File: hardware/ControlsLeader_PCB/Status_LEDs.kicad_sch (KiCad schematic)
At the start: 0 parts

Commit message: Schematic Backup
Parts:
- added D1, D10, D11, D12, D13, D14, D15, D2, D3, D4, D5, D6, D7, D8, D9: 0805_SMD, symbol Device:LED
- added D16: Controls_PWR, symbol Device:LED
- added D18: BPS_Fault, symbol Device:LED
- added D19: Controls_HB, symbol Device:LED
- added R30, R33, R34, R35, R36, R37, R38, R39, R40, R41, R42, R43, R44, R45, R46, R47, R49, R50: 10.6k, symbol Device:R
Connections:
- new net: D12.1 (K), R43.1
- new net: D5.1 (K), R36.1
- new net: D6.1 (K), R37.1
- new net: D2.1 (K), R33.1
- new net: D19.1 (K), R50.1
- new net: D4.1 (K), R35.1
- new net: D9.1 (K), R40.1
- new net: D15.1 (K), R46.1
- new net: D10.1 (K), R41.1
- new net: D7.1 (K), R38.1
- new net: D18.1 (K), R49.1
- new net: D11.1 (K), R42.1
- new net: D8.1 (K), R39.1
- new net: D14.1 (K), R45.1
- new net: D16.1 (K), R47.1
- new net: D13.1 (K), R44.1
- new net: D3.1 (K), R34.1
- new net: D1.1 (K), R30.1
- new net BPS_Fault_PWM: D16.2 (A), D18.2 (A), D19.2 (A)
- new net Cruise_Enable_GPIO_IN: D13.2 (A)
- new net Cruise_Set_GPIO_IN: D12.2 (A)
- new net Fwd_SW_GPIO: D3.2 (A)
- new net GND: R30.2, R33.2, R34.2, R35.2, R36.2, R37.2, R38.2, R39.2, R40.2, R41.2, R42.2, R43.2, R44.2, R45.2, R46.2, R47.2, R49.2, R50.2
- new net Hazard_GPIO_IN: D15.2 (A)
- new net Horn_24V_Signal_Out: D7.2 (A)
- new net Horn_GPIO_IN: D8.2 (A)
- new net Horn_GPIO_OUT: D9.2 (A)
- new net Ign_OFF_GPIO: D6.2 (A)
- new net Ign_arr_GPIO: D1.2 (A)
- new net Ign_mtr_GPIO: D2.2 (A)
- new net Left_Blinker_ON: D10.2 (A)
- new net Neutral_Gear_GPIO: D5.2 (A)
- new net Regen_Enable_GPIO_IN: D14.2 (A)
- new net Rev_SW_GPIO: D4.2 (A)
- new net Right_Blinker_ON: D11.2 (A)

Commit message: DONE!!! - just need to add footprints + part #s)
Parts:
- removed D19: Controls_HB, symbol Device:LED
- removed R49, R50: 10.6k, symbol Device:R
- added 3.3V1: TestPoint, TestPoint:TestPoint_Pad_1.0x1.0mm, symbol Connector:TestPoint
- added C15, C16: 10uF, Capacitor_SMD:C_0805_2012Metric_Pad1.18x1.45mm_HandSolder, symbol Device:C
- added D17, D26, D27, D28, D29: 0603_SMD, symbol Device:LED
- added J5: BPS_Fault_LED, Connector_Molex:Molex_Micro-Fit_3.0_43650-0300_1x03_P3.00mm_Horizontal, symbol Connector_Generic:Conn_01x03
- added R16, R17: 20, symbol Device:R
- added R55, R56, R57, R58: 120, symbol Device:R
- added U4: LT1963AEST-3.3#TRPBF, Package_TO_SOT_SMD:SOT-223-3_TabPin2, symbol Regulator_Linear:LT1963AxST-3.3
- D1, D10, D11, D12, D13, D14, D15, D2, D3, D4, D5, D6, D7, D8, D9: value 0805_SMD -> 0603_SMD
- D16: value Controls_PWR -> 0603_SMD
- D18: value BPS_Fault -> 0603_SMD
- R30, R33, R34, R35, R36, R37, R38, R39, R40, R41, R42, R43, R44: value 10.6k -> 20
- R45, R46: value 10.6k -> 120
- R47: value 10.6k -> 1.1k
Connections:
- net GND: now also C15.2, C16.2, J5.1 (Pin_1), R16.2, R17.2, R55.2, R56.2, R57.2, R58.2, U4.2 (GND)
- net at D12.1 (K): now also R41.1; no longer R43.1
- net at R36.1: now also D7.1 (K); no longer D5.1 (K)
- net at D6.1 (K): now also R35.1; no longer R37.1
- net at D2.1 (K): now also R16.1; no longer R33.1
- net at D4.1 (K): now also R33.1; no longer R35.1
- net at D9.1 (K): now also R38.1; no longer R40.1
- net at R46.1: now also D18.1 (K); no longer D15.1 (K)
- net at D10.1 (K): now also R39.1; no longer R41.1
- net at D11.1 (K): now also R40.1; no longer R42.1
- net at D8.1 (K): now also R37.1; no longer R39.1
- net at R45.1: now also D17.1 (K); no longer D14.1 (K)
- net at R44.1: now also D15.1 (K); no longer D13.1 (K)
- net at D3.1 (K): now also R17.1; no longer R34.1
- net BPS_Fault_PWM renamed Controls_PWR
- net Controls_PWR: no longer D18.2 (A)
- new net: D28.1 (K), R57.1
- new net: D27.1 (K), R56.1
- new net: D26.1 (K), R55.1
- new net: D29.1 (K), R58.1
- new net: D5.1 (K), R34.1
- new net: D14.1 (K), R43.1
- new net: D13.1 (K), R42.1
- new net +3V3: 3.3V1.1, C16.1, J5.3 (Pin_3), U4.3 (OUT)
- new net +5V: C15.1, U4.1 (IN)
- new net Extra_LED1: D17.2 (A)
- new net Extra_LED2: D18.2 (A)
- new net Extra_LED3: D26.2 (A)
- new net Extra_LED4: D27.2 (A)
- new net Extra_LED5: D28.2 (A)
- new net Extra_LED6: D29.2 (A)
- new net Indicator_PWM: J5.2 (Pin_2)
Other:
- note added: "5 -> 3.3v LDO"
- note added: "Controls PWR Status (red)"
- note added: "Dash Status Lights"
- note added: "Extra Programmable Status LEDs (green)"
- note added: "GPIO Status LEDs (blue)"
- note added: "Max current: 1.5A"
- moved on the sheet: D1, D16, R30, R47

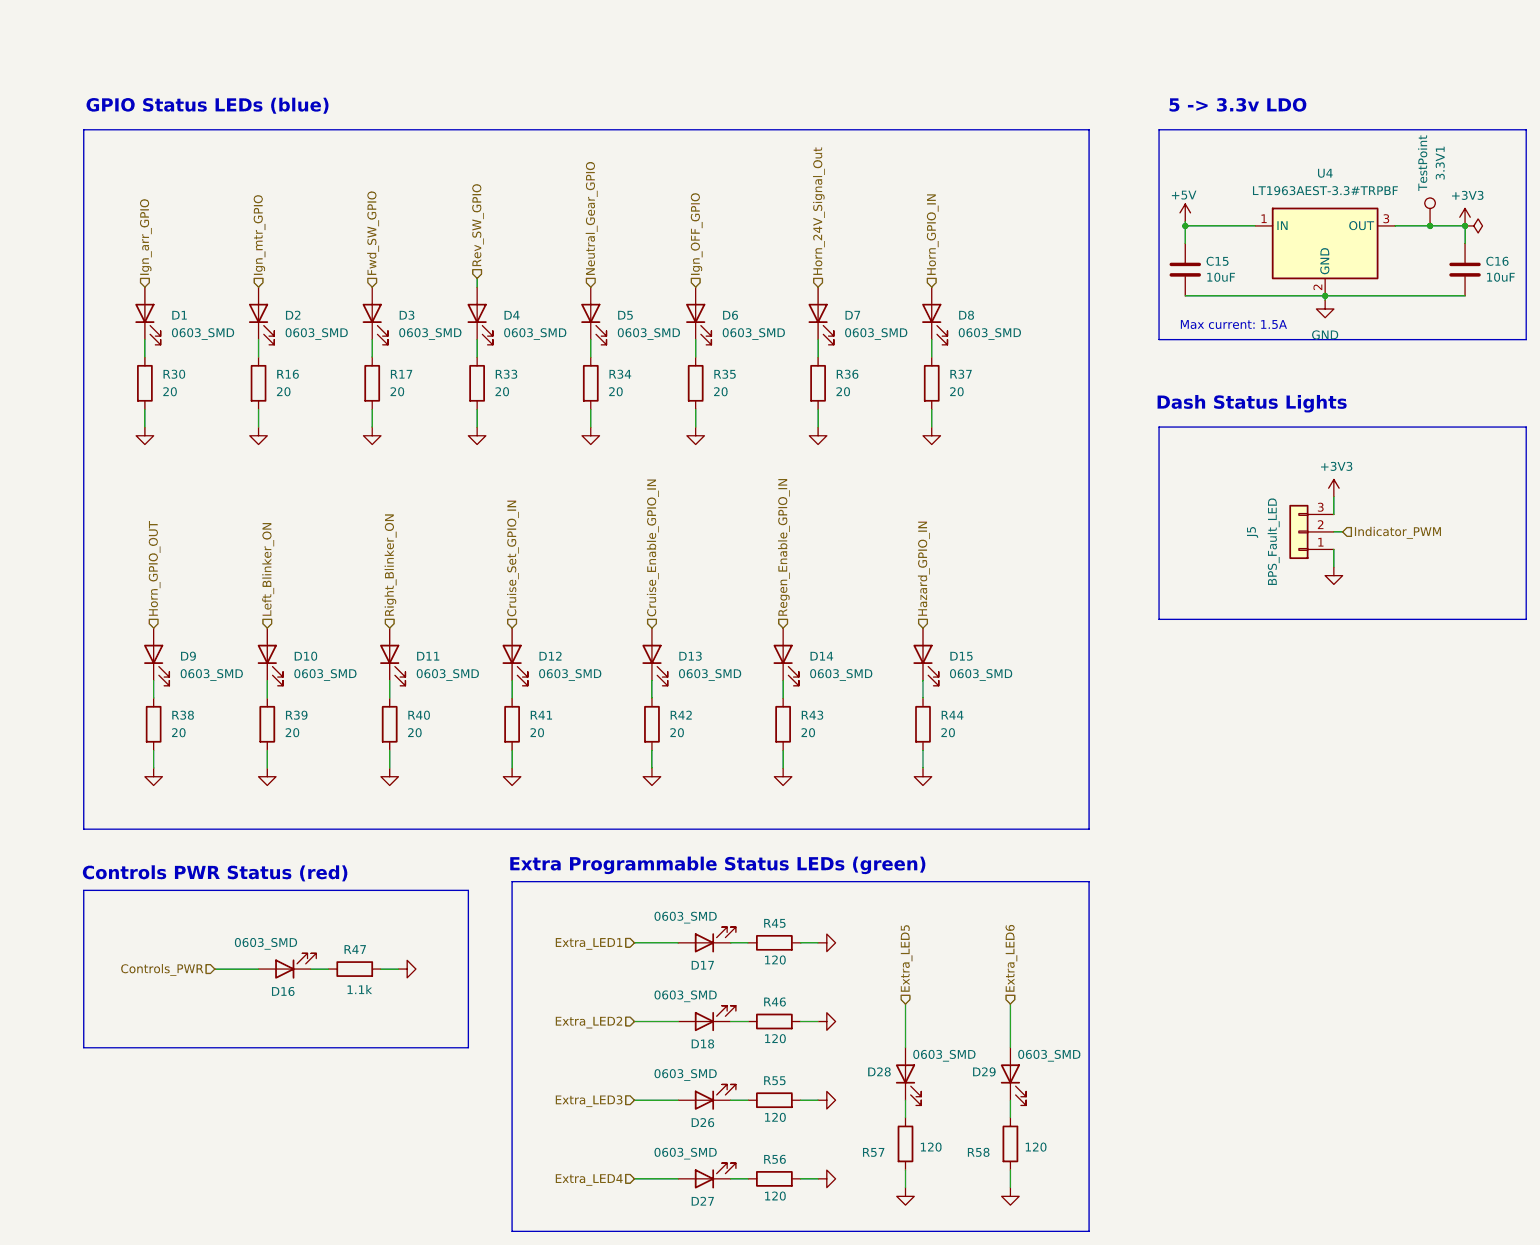
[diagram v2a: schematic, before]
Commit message: Schematic Ready for Review - Just need FET footprints to be confirmed
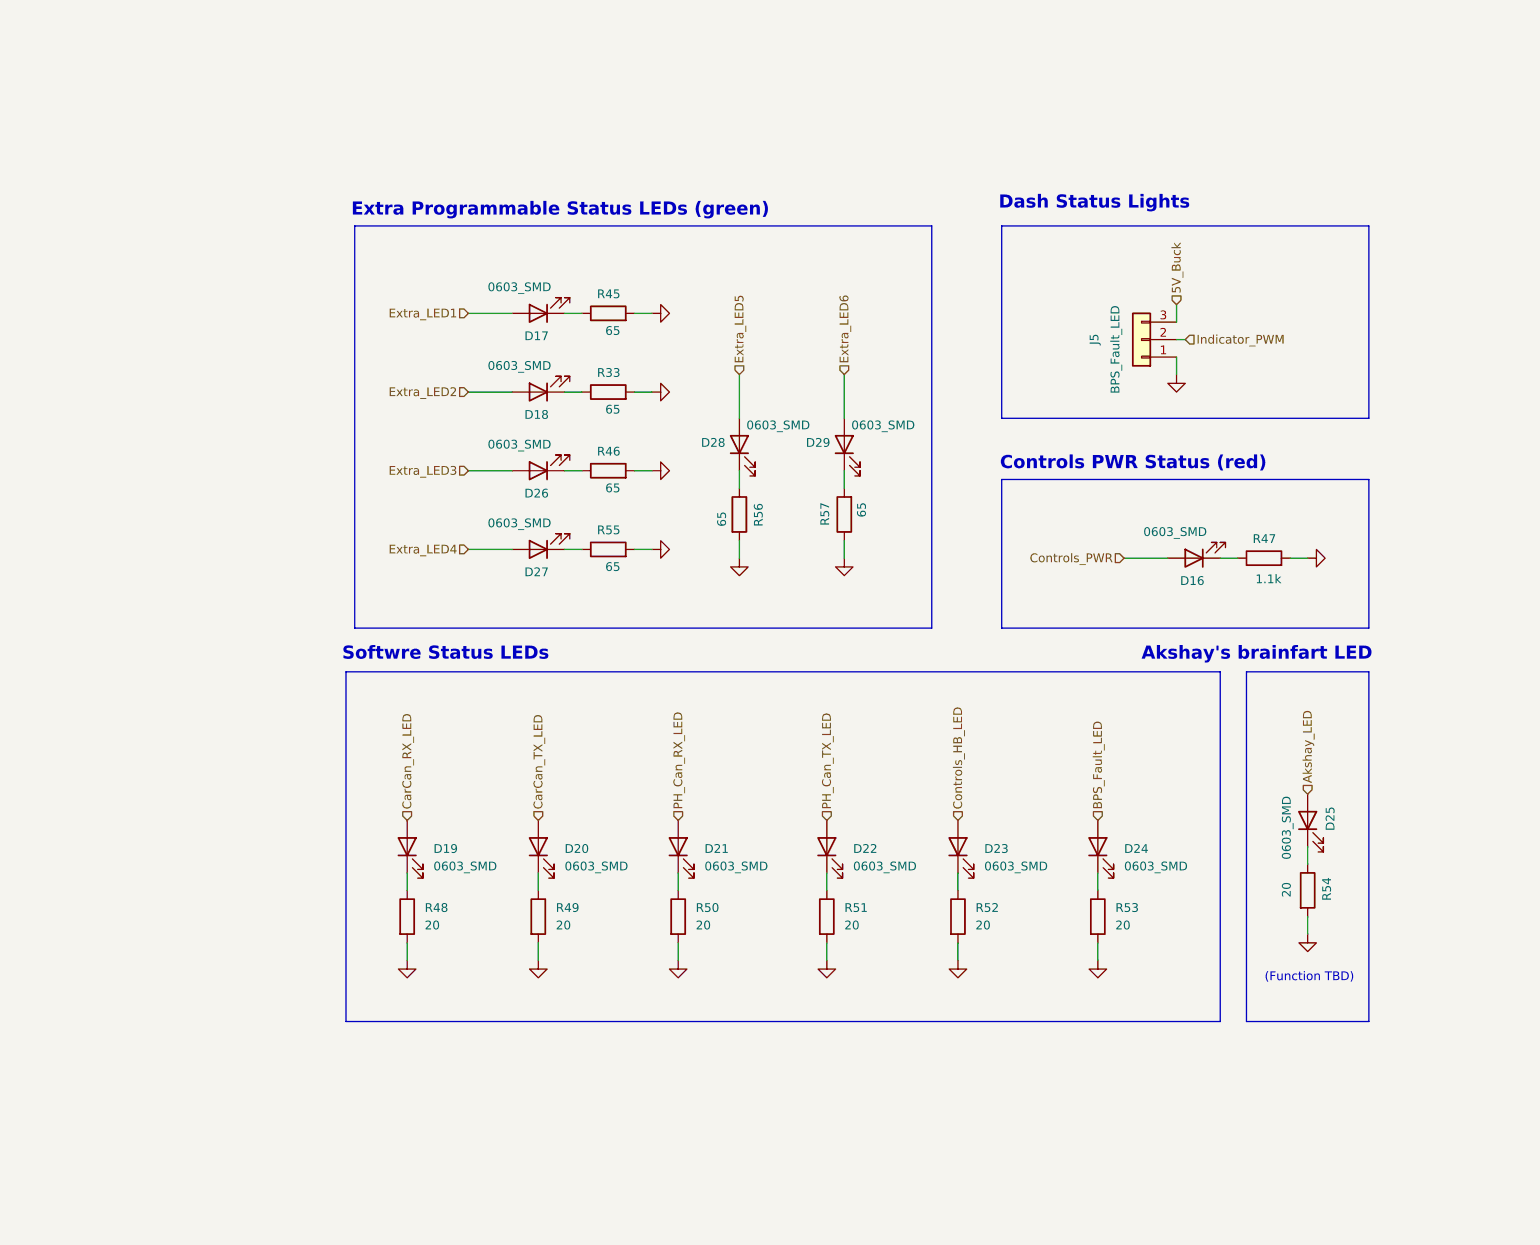
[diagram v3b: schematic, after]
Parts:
- removed 3.3V1: TestPoint, TestPoint:TestPoint_Pad_1.0x1.0mm, symbol Connector:TestPoint
- removed C15, C16: 10uF, Capacitor_SMD:C_0805_2012Metric_Pad1.18x1.45mm_HandSolder, symbol Device:C
- removed D1, D10, D11, D12, D13, D14, D15, D2, D3, D4, D5, D6, D7, D8, D9: 0603_SMD, symbol Device:LED
- removed R16, R17, R30, R34, R35, R36, R37, R38, R39, R40, R41, R42, R43, R44: 20, symbol Device:R
- removed R58: 120, symbol Device:R
- removed U4: LT1963AEST-3.3#TRPBF, Package_TO_SOT_SMD:SOT-223-3_TabPin2, symbol Regulator_Linear:LT1963AxST-3.3
- added D19, D20, D21, D22, D23, D24, D25: 0603_SMD, LED_SMD:LED_0201_0603Metric_Pad0.64x0.40mm_HandSolder, symbol Device:LED
- added R48, R49, R50, R51, R52, R53, R54: 20, Capacitor_SMD:C_0201_0603Metric_Pad0.64x0.40mm_HandSolder, symbol Device:R
- D16, D17, D18, D26, D27, D28, D29: footprint (none) -> LED_SMD:LED_0201_0603Metric_Pad0.64x0.40mm_HandSolder
- R33: value 20 -> 65; footprint (none) -> Capacitor_SMD:C_0201_0603Metric_Pad0.64x0.40mm_HandSolder
- R45, R46, R55, R56, R57: value 120 -> 65; footprint (none) -> Capacitor_SMD:C_0201_0603Metric_Pad0.64x0.40mm_HandSolder
- R47: footprint (none) -> Capacitor_SMD:C_0201_0603Metric_Pad0.64x0.40mm_HandSolder
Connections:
- net GND: now also R57.1, R48.2, R49.2, R50.2, R51.2, R52.2, R53.2, R54.2; no longer R57.2
- net at D18.1 (K): now also R33.1; no longer R46.1
- net at D28.1 (K): now also R56.1; no longer R57.1
- net at D27.1 (K): now also R55.1; no longer R56.1
- net at D26.1 (K): now also R46.1; no longer R55.1
- net at D29.1 (K): now also R57.2
- net +3V3 renamed 5V_Buck
- new net: D23.1 (K), R52.1
- new net: D25.1 (K), R54.1
- new net: D21.1 (K), R50.1
- new net: D22.1 (K), R51.1
- new net: D19.1 (K), R48.1
- new net: D20.1 (K), R49.1
- new net: D24.1 (K), R53.1
- new net Akshay_LED: D25.2 (A)
- new net BPS_Fault_LED: D24.2 (A)
- new net CarCan_RX_LED: D19.2 (A)
- new net CarCan_TX_LED: D20.2 (A)
- new net Controls_HB_LED: D23.2 (A)
- new net PH_Can_RX_LED: D21.2 (A)
- new net PH_Can_TX_LED: D22.2 (A)
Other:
- note added: "(Function TBD)"
- note added: "Akshay's brainfart LED"
- note added: "Softwre Status LEDs"
- note removed: "5 -> 3.3v LDO"
- note removed: "GPIO Status LEDs (blue)"
- note removed: "Max current: 1.5A"
- moved on the sheet: D16, D17, D18, D26, D27, D28, D29, J5, R45, R47

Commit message: Ready for final review
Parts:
- D16: value 0603_SMD -> Controls_Leader_Status_Red; Distributor Link (none) -> https://www.digikey.com/en/products/detail/ams-osram-usa-in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; Manufacturer (none) -> DigiKey; Manufacturer Prt # (none) -> LS Q976.01-N1Q2-1-20-R18
- D17, D18, D19, D20, D21, D22, D23, D24, D25, D26, D27, D28, D29: Distributor Link (none) -> https://www.digikey.com/en/products/detail/ams-osram-usa-in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; Manufacturer (none) -> Digikey; Manufacturer Prt # (none) -> LG Q976.01-MGNI-35-1
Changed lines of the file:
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@@
 			)
 		)
-		(property "Distributor Link" ""
+		(property "Distributor Link" "https://www.digikey.com/en/products/detail/ams-osram-usa-inc/LG-Q976-01-MGNI-35-1/21556493"
 			(at 93.98 67.31 0)
 			(effects
@@
 			)
 		)
-		(property "Manufacturer" ""
+		(property "Manufacturer" "Digikey"
 			(at 93.98 67.31 0)
 			(effects
@@
 			)
 		)
-		(property "Manufacturer Prt #" ""
+		(property "Manufacturer Prt #" "LG Q976.01-MGNI-35-1"
 			(at 93.98 67.31 0)
 			(effects
@@
 			)
 		)
-		(property "Distributor Link" ""
+		(property "Distributor Link" "https://www.digikey.com/en/products/detail/ams-osram-usa-inc/LG-Q976-01-MGNI-35-1/21556493"
 			(at 205.74 129.54 0)
 			(effects
@@
 			)
 		)
-		(property "Manufacturer" ""
+		(property "Manufacturer" "Digikey"
 			(at 205.74 129.54 0)
 			(effects
@@
 			)
 		)
-		(property "Manufacturer Prt #" ""
+		(property "Manufacturer Prt #" "LG Q976.01-MGNI-35-1"
 			(at 205.74 129.54 0)
 			(effects
@@
 			)
 		)
-		(property "Distributor Link" ""
+		(property "Distributor Link" "https://www.digikey.com/en/products/detail/ams-osram-usa-inc/LG-Q976-01-MGNI-35-1/21556493"
 			(at 114.3 133.35 90)
 			(effects
@@
 			)
 		)
-		(property "Manufacturer" ""
+		(property "Manufacturer" "Digikey"
 			(at 114.3 133.35 90)
 			(effects
@@
 			)
 		)
-		(property "Manufacturer Prt #" ""
+		(property "Manufacturer Prt #" "LG Q976.01-MGNI-35-1"
 			(at 114.3 133.35 90)
 			(effects
@@
 			)
 		)
-		(property "Distributor Link" ""
+		(property "Distributor Link" "https://www.digikey.com/en/products/detail/ams-osram-usa-inc/LG-Q976-01-MGNI-35-1/21556493"
 			(at 135.89 133.35 90)
 			(effects
@@
 			)
 		)
-		(property "Manufacturer" ""
+		(property "Manufacturer" "Digikey"
 			(at 135.89 133.35 90)
 			(effects
@@
 			)
 		)
-		(property "Manufacturer Prt #" ""
+		(property "Manufacturer Prt #" "LG Q976.01-MGNI-35-1"
 			(at 135.89 133.35 90)
 			(effects
@@
 			)
 		)
-		(property "Distributor Link" ""
+		(property "Distributor Link" "https://www.digikey.com/en/products/detail/ams-osram-usa-inc/LG-Q976-01-MGNI-35-1/21556493"
 			(at 123.19 74.93 90)
 			(effects
@@
 			)
 		)
-		(property "Manufacturer" ""
+		(property "Manufacturer" "Digikey"
 			(at 123.19 74.93 90)
 			(effects
@@
 			)
 		)
-		(property "Manufacturer Prt #" ""
+		(property "Manufacturer Prt #" "LG Q976.01-MGNI-35-1"
 			(at 123.19 74.93 90)
 			(effects
@@
 			)
 		)
-		(property "Distributor Link" ""
+		(property "Distributor Link" "https://www.digikey.com/en/products/detail/ams-osram-usa-inc/LG-Q976-01-MGNI-35-1/21556493"
 			(at 74.93 133.35 90)
 			(effects
@@
 			)
 		)
-		(property "Manufacturer" ""
+		(property "Manufacturer" "Digikey"
 			(at 74.93 133.35 90)
 			(effects
@@
 			)
 		)
-		(property "Manufacturer Prt #" ""
+		(property "Manufacturer Prt #" "LG Q976.01-MGNI-35-1"
 			(at 74.93 133.35 90)
 			(effects
@@
 			)
 		)
-		(property "Distributor Link" ""
+		(property "Distributor Link" "https://www.digikey.com/en/products/detail/ams-osram-usa-inc/LG-Q976-01-MGNI-35-1/21556493"
 			(at 93.98 133.35 90)
 			(effects
@@
 			)
 		)
-		(property "Manufacturer" ""
+		(property "Manufacturer" "Digikey"
 			(at 93.98 133.35 90)
 			(effects
@@
 			)
 		)
-		(property "Manufacturer Prt #" ""
+		(property "Manufacturer Prt #" "LG Q976.01-MGNI-35-1"
 			(at 93.98 133.35 90)
 			(effects
@@
 			)
 		)
-		(property "Distributor Link" ""
+		(property "Distributor Link" "https://www.digikey.com/en/products/detail/ams-osram-usa-inc/LG-Q976-01-MGNI-35-1/21556493"
 			(at 138.43 74.93 90)
 			(effects
@@
 			)
 		)
-		(property "Manufacturer" ""
+		(property "Manufacturer" "Digikey"
 			(at 138.43 74.93 90)
 			(effects
@@
 			)
 		)
-		(property "Manufacturer Prt #" ""
+		(property "Manufacturer Prt #" "LG Q976.01-MGNI-35-1"
 			(at 138.43 74.93 90)
 			(effects
@@
 			)
 		)
-		(property "Distributor Link" ""
+		(property "Distributor Link" "https://www.digikey.com/en/products/detail/ams-osram-usa-inc/LG-Q976-01-MGNI-35-1/21556493"
 			(at 175.26 133.35 90)
 			(effects
@@
 			)
 		)
-		(property "Manufacturer" ""
+		(property "Manufacturer" "Digikey"
 			(at 175.26 133.35 90)
 			(effects
@@
 			)
 		)
-		(property "Manufacturer Prt #" ""
+		(property "Manufacturer Prt #" "LG Q976.01-MGNI-35-1"
 			(at 175.26 133.35 90)
 			(effects
@@
 			)
 		)
-		(property "Value" "0603_SMD"
-			(at 181.864 87.63 0)
+		(property "Value" "Controls_Leader_Status_Red"
+			(at 168.91 86.614 0)
 			(effects
 				(font
@@
 			)
 		)
-		(property "Distributor Link" ""
+		(property "Distributor Link" "https://www.digikey.com/en/products/detail/ams-osram-usa-inc/LS-Q976-01-N1Q2-1-20-R18/21556498"
 			(at 189.23 91.44 0)
 			(effects
@@
 			)
 		)
-		(property "Manufacturer" ""
+		(property "Manufacturer" "DigiKey"
 			(at 189.23 91.44 0)
 			(effects
@@
 			)
 		)
-		(property "Manufacturer Prt #" ""
+		(property "Manufacturer Prt #" "LS Q976.01-N1Q2-1-20-R18"
 			(at 189.23 91.44 0)
 			(effects
@@
 			)
 		)
-		(property "Distributor Link" ""
+		(property "Distributor Link" "https://www.digikey.com/en/products/detail/ams-osram-usa-inc/LG-Q976-01-MGNI-35-1/21556493"
 			(at 154.94 133.35 90)
 			(effects
@@
 			)
 		)
-		(property "Manufacturer" ""
+		(property "Manufacturer" "Digikey"
 			(at 154.94 133.35 90)
 			(effects
@@
 			)
 		)
-		(property "Manufacturer Prt #" ""
+		(property "Manufacturer Prt #" "LG Q976.01-MGNI-35-1"
 			(at 154.94 133.35 90)
 			(effects
@@
 			)
 		)
-		(property "Distributor Link" ""
+		(property "Distributor Link" "https://www.digikey.com/en/products/detail/ams-osram-usa-inc/LG-Q976-01-MGNI-35-1/21556493"
 			(at 93.98 78.74 0)
 			(effects
@@
 			)
 		)
-		(property "Manufacturer" ""
+		(property "Manufacturer" "Digikey"
 			(at 93.98 78.74 0)
 			(effects
@@
 			)
 		)
-		(property "Manufacturer Prt #" ""
+		(property "Manufacturer Prt #" "LG Q976.01-MGNI-35-1"
 			(at 93.98 78.74 0)
 			(effects
@@
 			)
 		)
-		(property "Distributor Link" ""
+		(property "Distributor Link" "https://www.digikey.com/en/products/detail/ams-osram-usa-inc/LG-Q976-01-MGNI-35-1/21556493"
 			(at 93.98 90.17 0)
 			(effects
@@
 			)
 		)
-		(property "Manufacturer" ""
+		(property "Manufacturer" "Digikey"
 			(at 93.98 90.17 0)
 			(effects
@@
 			)
 		)
-		(property "Manufacturer Prt #" ""
+		(property "Manufacturer Prt #" "LG Q976.01-MGNI-35-1"
 			(at 93.98 90.17 0)
 			(effects
@@
 			)
 		)
-		(property "Distributor Link" ""
+		(property "Distributor Link" "https://www.digikey.com/en/products/detail/ams-osram-usa-inc/LG-Q976-01-MGNI-35-1/21556493"
 			(at 93.98 55.88 0)
 			(effects
@@
 			)
 		)
-		(property "Manufacturer" ""
+		(property "Manufacturer" "Digikey"
 			(at 93.98 55.88 0)
 			(effects
@@
 			)
 		)
-		(property "Manufacturer Prt #" ""
+		(property "Manufacturer Prt #" "LG Q976.01-MGNI-35-1"
 			(at 93.98 55.88 0)
 			(effects
@@
 			(at 181.61 59.69 0)
 			(effects
-				(font
-					(size 1.27 1.27)
-				)
-				(hide yes)
-			)
-		)
-		(property "Link" ""
-			(at 181.61 59.69 0)
-			(effects
